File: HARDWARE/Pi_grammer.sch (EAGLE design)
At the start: 27 parts, among them J1 AVR_SPI_PROG_3X22X3_LOCK, U1 AT42QT1010SOT23

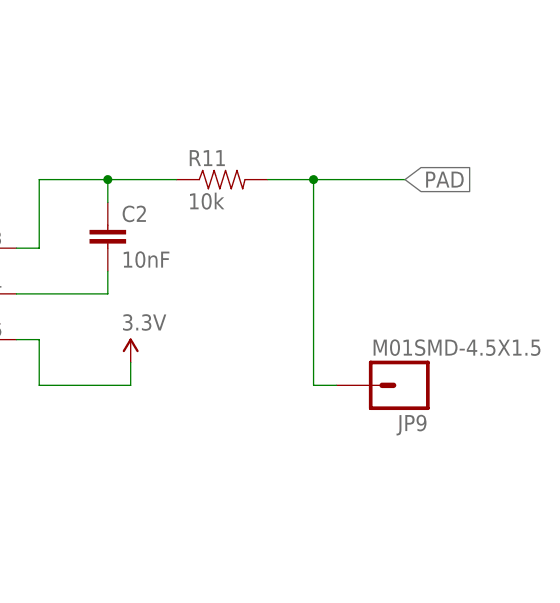
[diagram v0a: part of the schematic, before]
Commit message: Corrected capsense pad to be on top layer
whoops
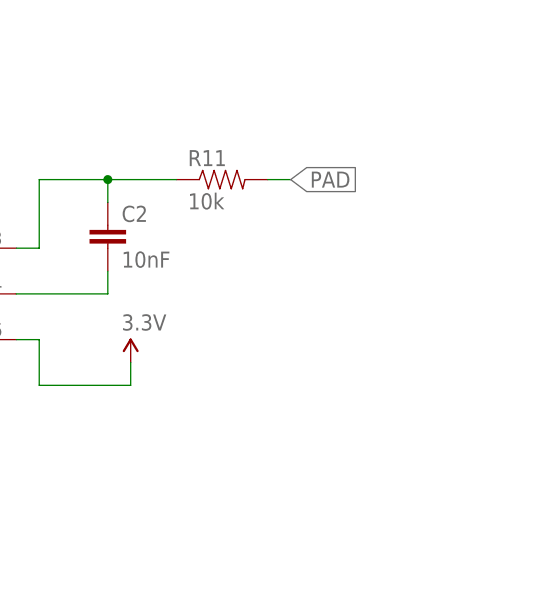
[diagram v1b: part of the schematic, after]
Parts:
- removed JP9: M01SMD-4.5X1.5, SparkFun-Connectors:M01SMD-4.5X1.5
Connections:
- net PAD: no longer JP9.1
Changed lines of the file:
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@@
 <grid distance="0.1" unitdist="inch" unit="inch" style="lines" multiple="1" display="no" altdistance="0.01" altunitdist="inch" altunit="inch"/>
 <layers>
-<layer number="1" name="Top" color="4" fill="1" visible="yes" active="no"/>
-<layer number="2" name="Route2" color="1" fill="3" visible="yes" active="no"/>
-<layer number="3" name="Route3" color="4" fill="3" visible="yes" active="no"/>
-<layer number="4" name="Route4" color="1" fill="4" visible="yes" active="no"/>
-<layer number="5" name="Route5" color="4" fill="4" visible="yes" active="no"/>
-<layer number="6" name="Route6" color="1" fill="8" visible="yes" active="no"/>
-<layer number="7" name="Route7" color="4" fill="8" visible="yes" active="no"/>
-<layer number="8" name="Route8" color="1" fill="2" visible="yes" active="no"/>
-<layer number="9" name="Route9" color="4" fill="2" visible="yes" active="no"/>
-<layer number="10" name="Route10" color="1" fill="7" visible="yes" active="no"/>
-<layer number="11" name="Route11" color="4" fill="7" visible="yes" active="no"/>
-<layer number="12" name="Route12" color="1" fill="5" visible="yes" active="no"/>
-<layer number="13" name="Route13" color="4" fill="5" visible="yes" active="no"/>
-<layer number="14" name="Route14" color="1" fill="6" visible="yes" active="no"/>
-<layer number="15" name="Route15" color="4" fill="6" visible="yes" active="no"/>
-<layer number="16" name="Bottom" color="1" fill="1" visible="yes" active="no"/>
-<layer number="17" name="Pads" color="2" fill="1" visible="yes" active="no"/>
-<layer number="18" name="Vias" color="2" fill="1" visible="yes" active="no"/>
-<layer number="19" name="Unrouted" color="6" fill="1" visible="yes" active="no"/>
-<layer number="20" name="Dimension" color="15" fill="1" visible="yes" active="no"/>
-<layer number="21" name="tPlace" color="16" fill="1" visible="yes" active="no"/>
-<layer number="22" name="bPlace" color="14" fill="1" visible="yes" active="no"/>
-<layer number="23" name="tOrigins" color="15" fill="1" visible="yes" active="no"/>
-<layer number="24" name="bOrigins" color="15" fill="1" visible="yes" active="no"/>
-<layer number="25" name="tNames" color="7" fill="1" visible="yes" active="no"/>
-<layer number="26" name="bNames" color="7" fill="1" visible="yes" active="no"/>
-<layer number="27" name="tValues" color="7" fill="1" visible="yes" active="no"/>
-<layer number="28" name="bValues" color="7" fill="1" visible="yes" active="no"/>
+<layer number="1" name="Top" color="4" fill="1" visible="no" active="no"/>
+<layer number="2" name="Route2" color="1" fill="3" visible="no" active="no"/>
+<layer number="3" name="Route3" color="4" fill="3" visible="no" active="no"/>
+<layer number="4" name="Route4" color="1" fill="4" visible="no" active="no"/>
+<layer number="5" name="Route5" color="4" fill="4" visible="no" active="no"/>
+<layer number="6" name="Route6" color="1" fill="8" visible="no" active="no"/>
+<layer number="7" name="Route7" color="4" fill="8" visible="no" active="no"/>
+<layer number="8" name="Route8" color="1" fill="2" visible="no" active="no"/>
+<layer number="9" name="Route9" color="4" fill="2" visible="no" active="no"/>
+<layer number="10" name="Route10" color="1" fill="7" visible="no" active="no"/>
+<layer number="11" name="Route11" color="4" fill="7" visible="no" active="no"/>
+<layer number="12" name="Route12" color="1" fill="5" visible="no" active="no"/>
+<layer number="13" name="Route13" color="4" fill="5" visible="no" active="no"/>
+<layer number="14" name="Route14" color="1" fill="6" visible="no" active="no"/>
+<layer number="15" name="Route15" color="4" fill="6" visible="no" active="no"/>
+<layer number="16" name="Bottom" color="1" fill="1" visible="no" active="no"/>
+<layer number="17" name="Pads" color="2" fill="1" visible="no" active="no"/>
+<layer number="18" name="Vias" color="2" fill="1" visible="no" active="no"/>
+<layer number="19" name="Unrouted" color="6" fill="1" visible="no" active="no"/>
+<layer number="20" name="Dimension" color="15" fill="1" visible="no" active="no"/>
+<layer number="21" name="tPlace" color="16" fill="1" visible="no" active="no"/>
+<layer number="22" name="bPlace" color="14" fill="1" visible="no" active="no"/>
+<layer number="23" name="tOrigins" color="15" fill="1" visible="no" active="no"/>
+<layer number="24" name="bOrigins" color="15" fill="1" visible="no" active="no"/>
+<layer number="25" name="tNames" color="7" fill="1" visible="no" active="no"/>
+<layer number="26" name="bNames" color="7" fill="1" visible="no" active="no"/>
+<layer number="27" name="tValues" color="7" fill="1" visible="no" active="no"/>
+<layer number="28" name="bValues" color="7" fill="1" visible="no" active="no"/>
 <layer number="29" name="tStop" color="7" fill="3" visible="no" active="no"/>
 <layer number="30" name="bStop" color="7" fill="6" visible="no" active="no"/>
@@
 <layer number="35" name="tGlue" color="7" fill="4" visible="no" active="no"/>
 <layer number="36" name="bGlue" color="7" fill="5" visible="no" active="no"/>
-<layer number="37" name="tTest" color="7" fill="1" visible="yes" active="no"/>
-<layer number="38" name="bTest" color="7" fill="1" visible="yes" active="no"/>
+<layer number="37" name="tTest" color="7" fill="1" visible="no" active="no"/>
+<layer number="38" name="bTest" color="7" fill="1" visible="no" active="no"/>
 <layer number="39" name="tKeepout" color="4" fill="11" visible="no" active="no"/>
 <layer number="40" name="bKeepout" color="1" fill="11" visible="no" active="no"/>
@@
 <layer number="44" name="Drills" color="7" fill="1" visible="no" active="no"/>
 <layer number="45" name="Holes" color="7" fill="1" visible="no" active="no"/>
-<layer number="46" name="Milling" color="3" fill="1" visible="yes" active="no"/>
-<layer number="47" name="Measures" color="7" fill="1" visible="yes" active="no"/>
-<layer number="48" name="Document" color="7" fill="1" visible="yes" active="no"/>
-<layer number="49" name="Reference" color="7" fill="1" visible="yes" active="no"/>
-<layer number="50" name="dxf" color="7" fill="1" visible="yes" active="no"/>
-<layer number="51" name="tDocu" color="6" fill="1" visible="yes" active="no"/>
-<layer number="52" name="bDocu" color="7" fill="1" visible="yes" active="no"/>
-<layer number="53" name="tGND_GNDA" color="7" fill="9" visible="yes" active="no"/>
-<layer number="54" name="bGND_GNDA" color="1" fill="9" visible="yes" active="no"/>
-<layer number="56" name="wert" color="7" fill="1" visible="yes" active="no"/>
-<layer number="57" name="tCAD" color="7" fill="1" visible="yes" active="no"/>
-<layer number="59" name="tCarbon" color="7" fill="1" visible="yes" active="no"/>
-<layer number="60" name="bCarbon" color="7" fill="1" visible="yes" active="no"/>
+<layer number="46" name="Milling" color="3" fill="1" visible="no" active="no"/>
+<layer number="47" name="Measures" color="7" fill="1" visible="no" active="no"/>
+<layer number="48" name="Document" color="7" fill="1" visible="no" active="no"/>
+<layer number="49" name="Reference" color="7" fill="1" visible="no" active="no"/>
+<layer number="50" name="dxf" color="7" fill="1" visible="no" active="no"/>
+<layer number="51" name="tDocu" color="6" fill="1" visible="no" active="no"/>
+<layer number="52" name="bDocu" color="7" fill="1" visible="no" active="no"/>
+<layer number="53" name="tGND_GNDA" color="7" fill="9" visible="no" active="no"/>
+<layer number="54" name="bGND_GNDA" color="1" fill="9" visible="no" active="no"/>
+<layer number="56" name="wert" color="7" fill="1" visible="no" active="no"/>
+<layer number="57" name="tCAD" color="7" fill="1" visible="no" active="no"/>
+<layer number="59" name="tCarbon" color="7" fill="1" visible="no" active="no"/>
+<layer number="60" name="bCarbon" color="7" fill="1" visible="no" active="no"/>
 <layer number="90" name="Modules" color="5" fill="1" visible="yes" active="yes"/>
 <layer number="91" name="Nets" color="2" fill="1" visible="yes" active="yes"/>
@@
 <part name="GND3" library="SparkFun-Aesthetics" deviceset="GND" device=""/>
 <part name="GND5" library="SparkFun-Aesthetics" deviceset="GND" device=""/>
-<part name="JP9" library="SparkFun-Connectors" deviceset="M01" device="SMD-4.5X1.5"/>
 <part name="SUPPLY4" library="SparkFun-Aesthetics" deviceset="3.3V" device=""/>
 <part name="SUPPLY6" library="SparkFun-Aesthetics" deviceset="3.3V" device=""/>
@@
 <instance part="GND3" gate="1" x="210.82" y="63.5"/>
 <instance part="GND5" gate="1" x="236.22" y="63.5"/>
-<instance part="JP9" gate="G$1" x="317.5" y="63.5" smashed="yes" rot="R180">
-<attribute name="VALUE" x="332.74" y="68.58" size="1.778" layer="96" rot="R180"/>
-<attribute name="NAME" x="320.04" y="60.198" size="1.778" layer="95" rot="R180"/>
-</instance>
 <instance part="SUPPLY4" gate="G$1" x="256.54" y="91.44"/>
 <instance part="SUPPLY6" gate="G$1" x="210.82" y="78.74"/>
@@
 <segment>
 <pinref part="R11" gate="G$1" pin="2"/>
-<wire x1="302.26" y1="86.36" x2="307.34" y2="86.36" width="0.1524" layer="91"/>
-<wire x1="307.34" y1="86.36" x2="307.34" y2="63.5" width="0.1524" layer="91"/>
-<pinref part="JP9" gate="G$1" pin="1"/>
-<wire x1="307.34" y1="63.5" x2="309.88" y2="63.5" width="0.1524" layer="91"/>
-<wire x1="307.34" y1="86.36" x2="317.5" y2="86.36" width="0.1524" layer="91"/>
-<junction x="307.34" y="86.36"/>
-<label x="317.5" y="86.36" size="1.778" layer="95" xref="yes"/>
-</segment>
-</net>
+<wire x1="302.26" y1="86.36" x2="304.8" y2="86.36" width="0.1524" layer="91"/>
+<label x="304.8" y="86.36" size="1.778" layer="95" xref="yes"/>
+</segment>
+</net>

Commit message: Moved ICSP lines to a 1x6 connector
Also created adapter from 1x6 cable to 3x2 header
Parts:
- removed J1: AVR_SPI_PROG_3X22X3_LOCK, SparkFun-Connectors:AVR_SPI_PROG_3X22X3_LOCK
- added J2: TARGET_copy, SparkFun-Connectors:CONN_06POLAR
- added J3: TESTBED, SparkFun-Connectors:AVR_SPI_PROG_3X22X3_LOCK
- added J4: CABLE, SparkFun-Connectors:CONN_06RA
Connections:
- removed net GP18: J1.1, JP2.GP18#
- removed net GP19: J1.5, JP2.GP19
- removed net GP23: J1.4, JP2.GP23
- removed net GP24: J1.3, JP2.GP24
- new net GND_C: J3.6, J4.5
- new net MISO_C: J3.1, J4.2
- new net MISO_T: J2.2, JP2.GP18#
- new net MOSI_C: J3.4, J4.1
- new net MOSI_T: J2.1, JP2.GP23
- new net RST_C: J3.5, J4.4
- new net RST_T: J2.4, JP2.GP19
- new net SCK_C: J3.3, J4.3
- new net SCK_T: J2.3, JP2.GP24
- net GND: now also J2.5; no longer J1.6
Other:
- note added: "CONNECTOR 1x6 Cable >> 3x2 Female Header"

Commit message: PROD_IDs to all populated parts, SCH cleanup
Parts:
- added FRAME1: FRAME-LETTER, SparkFun-Aesthetics:FRAME-LETTER
- C1: device SparkFun-Capacitors:CAP0603-CAP -> SparkFun-Capacitors:0.1UF-25V(+80/-20%)(0603)
- C2: device SparkFun-Capacitors:CAP0603-CAP -> SparkFun-Capacitors:10NF/10000PF-50V-10%(0603)
- D1, D4, D5, D6, D7: device SparkFun-LED:LED1206 -> SparkFun-LED:LED-GREEN1206
- D2, D3, D8: device SparkFun-LED:LED1206 -> SparkFun-LED:LED-RED1206
- J2: PROD_ID (none) -> CONN-09698
- J3: PROD_ID (none) -> CONN-11566
- J4: PROD_ID (none) -> CONN-10140
- R1, R2, R3, R4, R5, R6, R8, R9: device SparkFun-Resistors:330OHM1/10W1%(0603) -> SparkFun-Resistors:1KOHM-1/10W-1%(0603)
- R11: device SparkFun-Resistors:RESISTOR0603 -> SparkFun-Resistors:10KOHM-1/10W-1%(0603)0603
- R7: device SparkFun-Resistors:330OHM1/10W1%(0603) -> SparkFun-Resistors:10KOHM-1/10W-1%(0603)0603
- U1: PROD_ID (none) -> IC-11778
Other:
- note added: "01"
- note added: "ADAPTER CONNECTOR 1x6 Cable >> 3x2 Female Header"
- note added: "Capsense trigger and shutdown button"
- note added: "Pete Lewis"
- note added: "Raspberry Pi 2x20 connector"
- note added: "Status LEDs"
- note removed: "CONNECTOR 1x6 Cable >> 3x2 Female Header"
- moved on the sheet: C1, C2, D1, D2, D3, D4, D5, D6, D7, D8, J2, J3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

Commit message: added fiducials
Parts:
- added FD1, FD2: FIDUCIALUFIDUCIAL, SparkFun-Aesthetics:FIDUCIALUFIDUCIAL
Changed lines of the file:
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@@
 <?xml version="1.0" encoding="utf-8"?>
 <!DOCTYPE eagle SYSTEM "eagle.dtd">
-<eagle version="6.5.0">
+<eagle version="7.6.0">
 <drawing>
 <settings>
@@
 </part>
 <part name="FRAME1" library="SparkFun-Aesthetics" deviceset="FRAME-LETTER" device=""/>
+<part name="FD1" library="SparkFun-Aesthetics" deviceset="FIDUCIAL" device="UFIDUCIAL"/>
+<part name="FD2" library="SparkFun-Aesthetics" deviceset="FIDUCIAL" device="UFIDUCIAL"/>
 </parts>
 <sheets>
@@
 <instance part="FRAME1" gate="G$1" x="7.62" y="182.88"/>
 <instance part="FRAME1" gate="V" x="154.94" y="182.88"/>
+<instance part="FD1" gate="G$1" x="248.92" y="208.28"/>
+<instance part="FD2" gate="G$1" x="254" y="215.9"/>
 </instances>
 <busses>

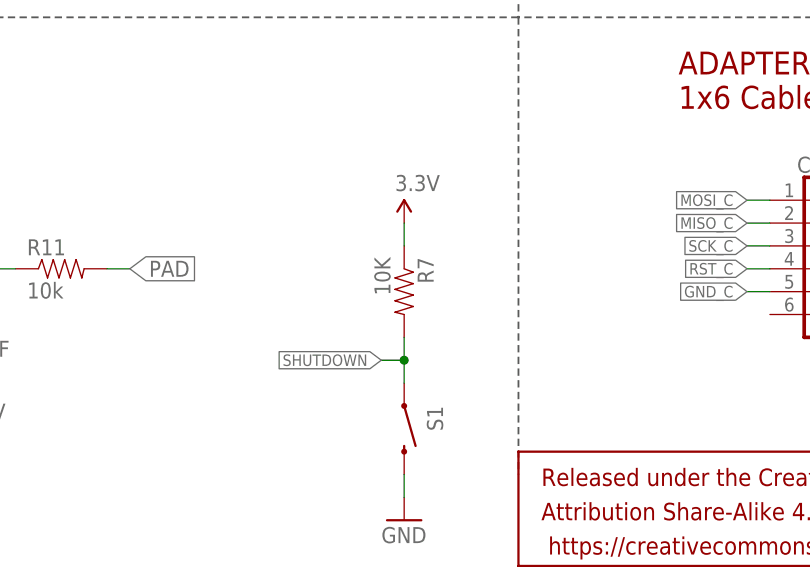
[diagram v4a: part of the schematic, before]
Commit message: Changed value of R7 to 1K
This is the pullup resistor on the SHUTDOWN line/button. I was seeing
some strange behavior on a few shields that would actually cause a
shutdown right at bootup. Getting a little more current on this pullup
seems to have solved the issue.
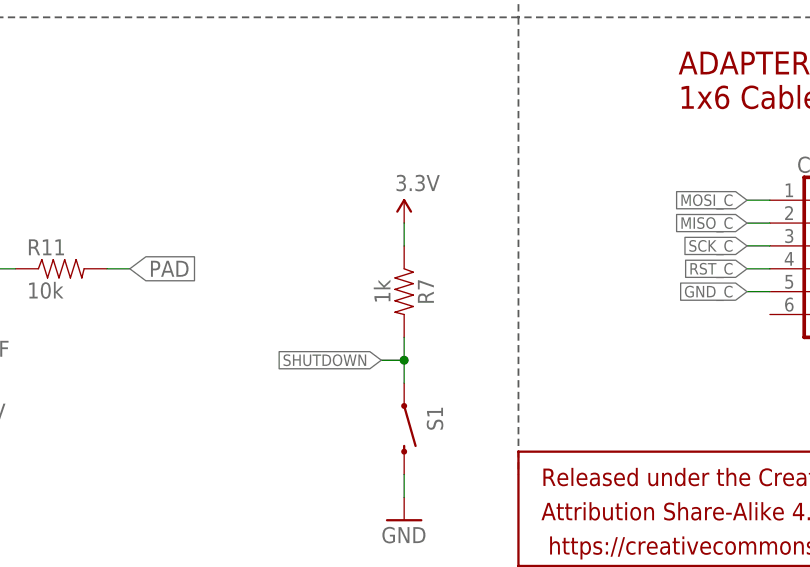
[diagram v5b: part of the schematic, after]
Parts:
- R7: value 10K -> 1k; device SparkFun-Resistors:10KOHM-1/10W-1%(0603)0603 -> SparkFun-Resistors:1KOHM-0603-1/10W-1%
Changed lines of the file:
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@@
 <part name="R6" library="SparkFun-Resistors" deviceset="1KOHM-1/10W-1%(0603)" device="" value="1K"/>
 <part name="S1" library="SparkFun-Electromechanical" deviceset="SWITCH-MOMENTARY-2" device="SMD" value=""/>
-<part name="R7" library="SparkFun-Resistors" deviceset="10KOHM-1/10W-1%(0603)" device="0603" value="10K"/>
+<part name="R7" library="SparkFun-Resistors" deviceset="1KOHM" device="-0603-1/10W-1%" value="1k"/>
 <part name="GND2" library="SparkFun" deviceset="GND" device=""/>
 <part name="SUPPLY1" library="SparkFun-Aesthetics" deviceset="3.3V" device=""/>
